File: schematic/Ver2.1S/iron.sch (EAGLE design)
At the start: 41 parts, among them IC1 LD117AS18TR, Q1 IRF4905, U1 STM32F103C8T, U3 OPAMP

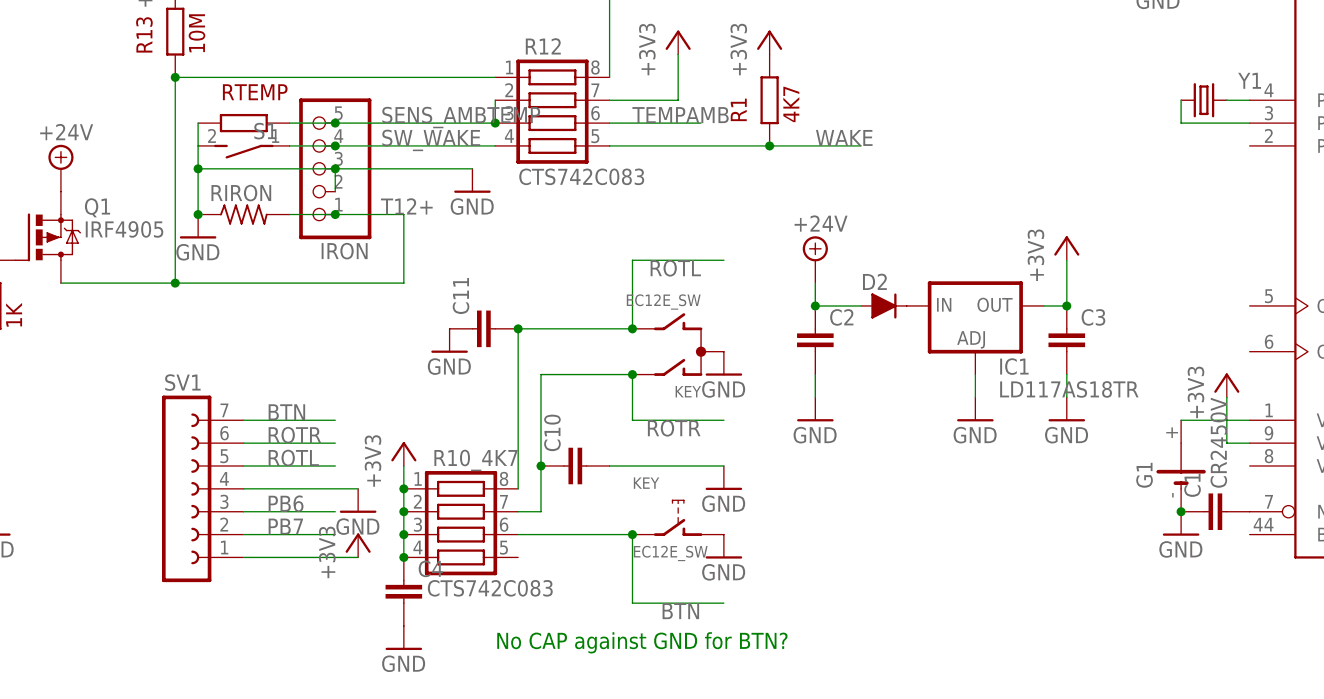
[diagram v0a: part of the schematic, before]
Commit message: schematics: minor rearrangements of some parts
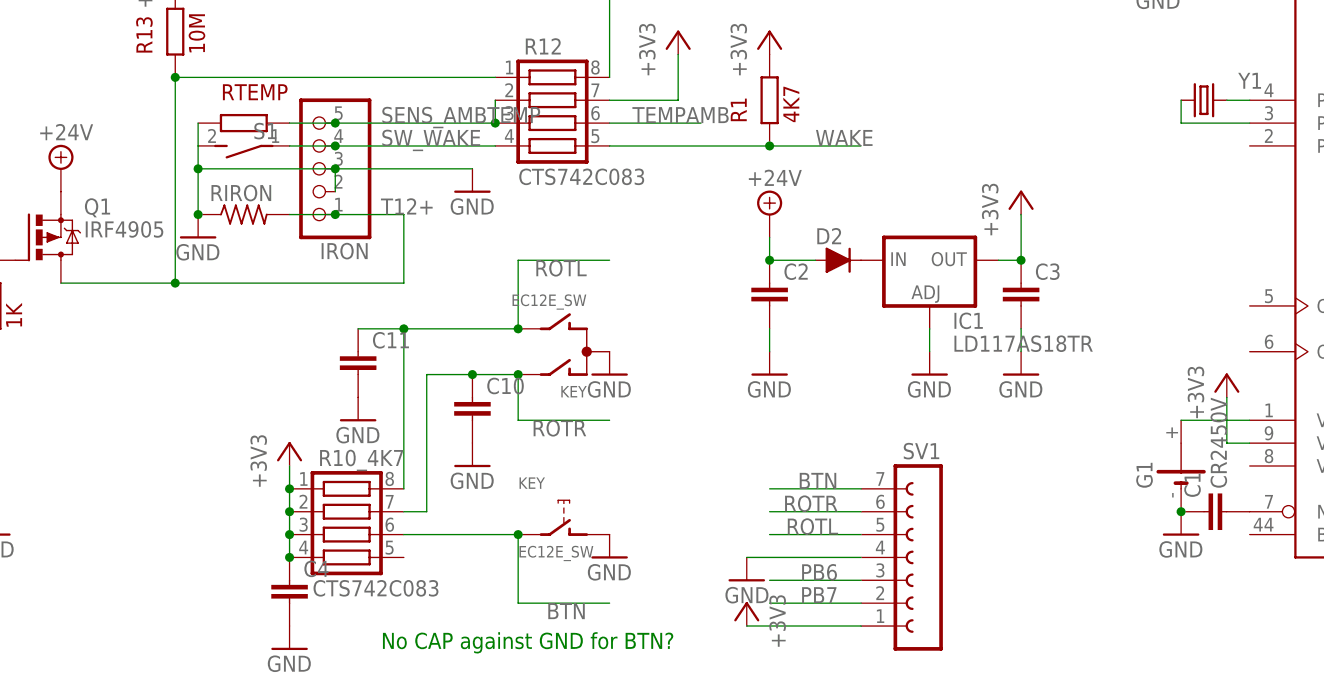
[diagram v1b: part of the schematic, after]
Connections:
- net GND: now also C11.2; no longer C11.1
- net ROTL: now also C11.1; no longer C11.2
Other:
- moved on the sheet: C10, C11, C2, C3, C4, D2, IC1, KEY, R10_4K7, SV1

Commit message: Ver2.1S some rearrangements
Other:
- moved on the sheet: G1
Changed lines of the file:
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@@
 <part name="GND23" library="supply1" library_urn="urn:adsk.eagle:library:371" deviceset="GND" device=""/>
 <part name="RIRON" library="resistor" library_urn="urn:adsk.eagle:library:348" deviceset="R-US_" device="0204/2V" package3d_urn="urn:adsk.eagle:package:25948/1"/>
+<part name="GND25" library="supply1" library_urn="urn:adsk.eagle:library:371" deviceset="GND" device=""/>
 </parts>
 <sheets>
@@
 <instance part="+3V7" gate="G$1" x="256.54" y="50.8" rot="MR0"/>
 <instance part="GND15" gate="1" x="266.7" y="43.18" rot="MR0"/>
-<instance part="G1" gate="1" x="154.94" y="-15.24" rot="R90"/>
-<instance part="+3V9" gate="G$1" x="160.02" y="-5.08"/>
+<instance part="G1" gate="1" x="157.48" y="-7.62"/>
+<instance part="+3V9" gate="G$1" x="147.32" y="-10.16"/>
 <instance part="DEBUG" gate="1" x="264.16" y="-7.62" rot="MR90"/>
 <instance part="GND17" gate="1" x="279.4" y="-5.08" rot="MR0"/>
@@
 <instance part="GND23" gate="1" x="45.72" y="10.16"/>
 <instance part="RIRON" gate="G$1" x="50.8" y="12.7"/>
+<instance part="GND25" gate="1" x="152.4" y="-10.16"/>
 </instances>
 <busses>
@@
 <pinref part="C1" gate="G$1" pin="1"/>
 <pinref part="GND14" gate="1" pin="GND"/>
-<pinref part="G1" gate="1" pin="-"/>
-<junction x="154.94" y="-20.32"/>
 </segment>
 <segment>
@@
 <pinref part="C11" gate="G$1" pin="2"/>
 <pinref part="GND21" gate="1" pin="GND"/>
+</segment>
+<segment>
+<pinref part="GND25" gate="1" pin="GND"/>
+<pinref part="G1" gate="1" pin="-"/>
+<wire x1="157.48" y1="-7.62" x2="152.4" y2="-7.62" width="0.1524" layer="91"/>
+<junction x="152.4" y="-7.62"/>
 </segment>
 </net>
@@
 <pinref part="+3V9" gate="G$1" pin="+3V3"/>
 <pinref part="U1" gate="MCU" pin="VDDA"/>
-<wire x1="160.02" y1="-7.62" x2="160.02" y2="-12.7" width="0.1524" layer="91"/>
-<wire x1="160.02" y1="-12.7" x2="162.56" y2="-12.7" width="0.1524" layer="91"/>
+<wire x1="147.32" y1="-12.7" x2="162.56" y2="-12.7" width="0.1524" layer="91"/>
 </segment>
 <segment>
@@
 </segment>
 </net>
-<net name="N$8" class="0">
-<segment>
-<pinref part="U1" gate="MCU" pin="VBAT"/>
-<pinref part="G1" gate="1" pin="+"/>
-<wire x1="154.94" y1="-10.16" x2="162.56" y2="-10.16" width="0.1524" layer="91"/>
-</segment>
-</net>
 <net name="DBG_DIO" class="0">
 <segment>
@@
 </segment>
 </net>
+<net name="N$8" class="0">
+<segment>
+<pinref part="U1" gate="MCU" pin="VBAT"/>
+<pinref part="G1" gate="1" pin="+"/>
+<wire x1="162.56" y1="-10.16" x2="162.56" y2="-7.62" width="0.1524" layer="91"/>
+</segment>
+</net>
